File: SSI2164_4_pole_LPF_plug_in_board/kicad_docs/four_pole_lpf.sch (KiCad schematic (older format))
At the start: 4 parts, among them J1 signal_in, J2 CV_in, J3 signal_out, J4 feedback_CV_and_power

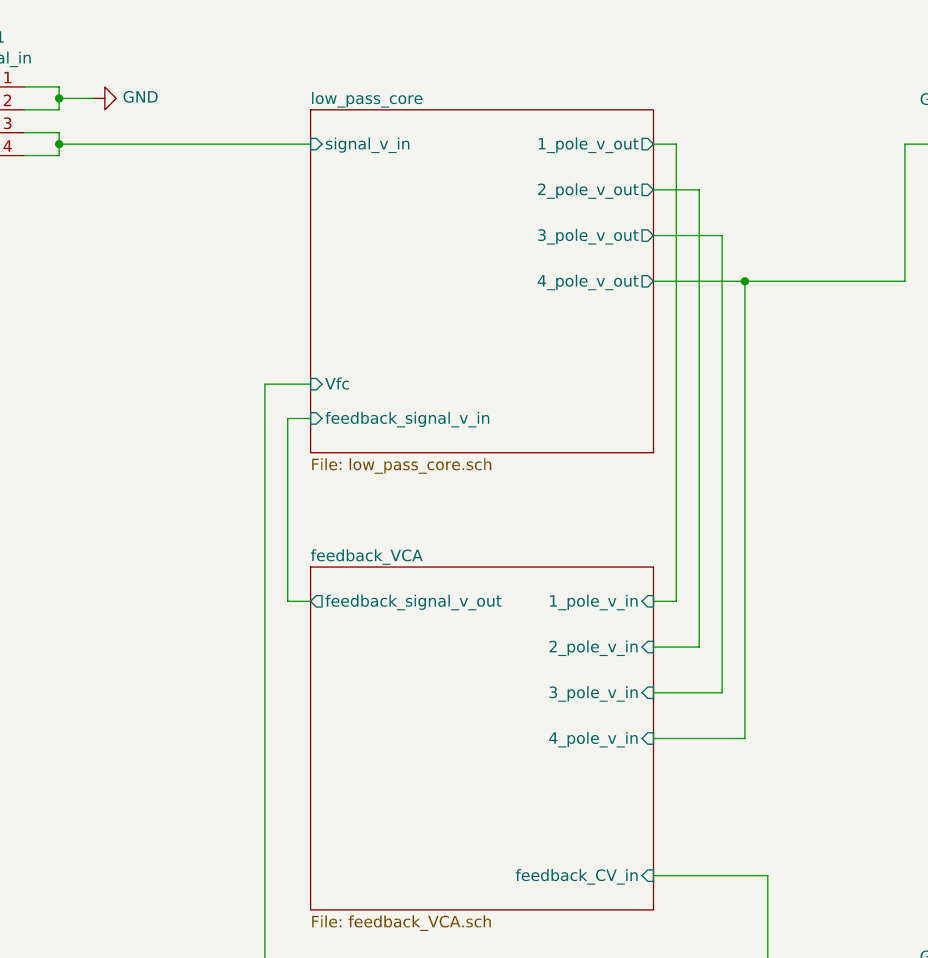
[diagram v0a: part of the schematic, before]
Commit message: progress on SSI2164 LPF
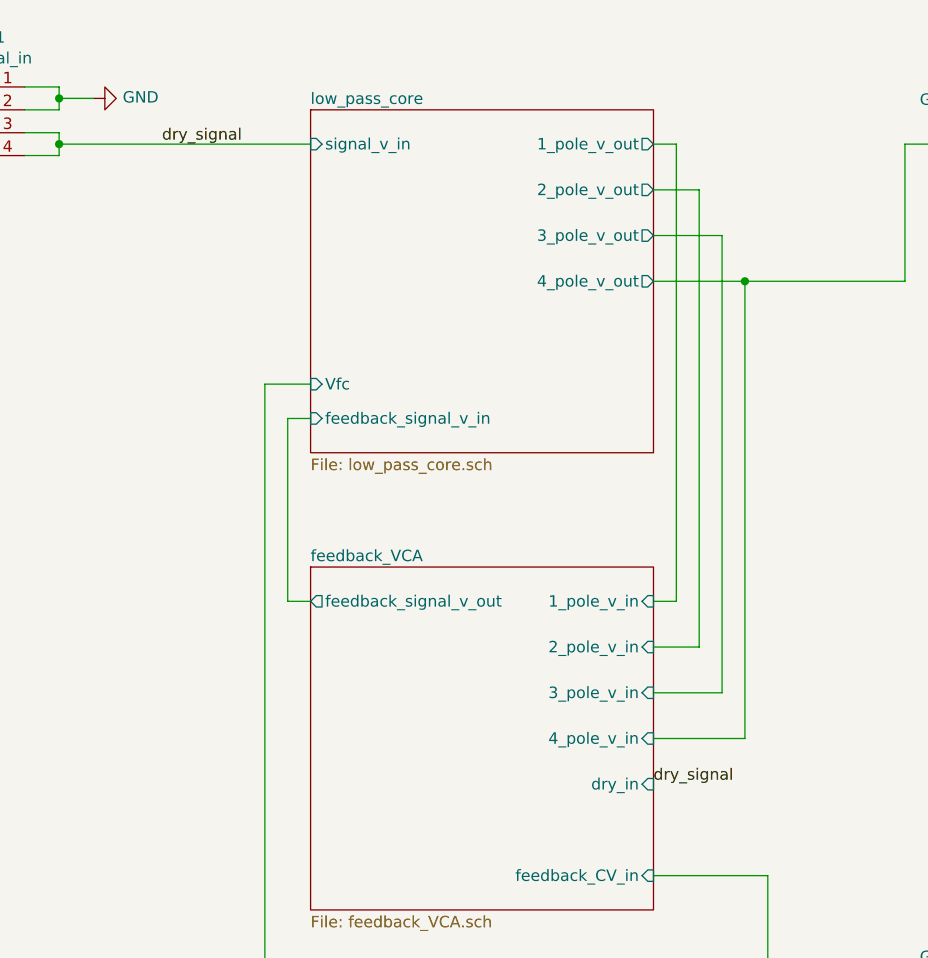
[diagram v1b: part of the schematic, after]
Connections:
- net low_pass_core/signal_v_in renamed dry_signal
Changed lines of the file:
@@
 F6 "feedback_signal_v_out" O L 4500 3650 50
 F7 "1_pole_v_in" I R 6000 3650 50
+F8 "dry_in" I R 6000 4450 50
 $EndSheet
+Text Label 6000 4450 0    50   ~ 0
+dry_signal
+Text Label 3850 1650 0    50   ~ 0
+dry_signal
 $EndSCHEMATC
